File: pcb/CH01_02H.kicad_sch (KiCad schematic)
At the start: 10 parts

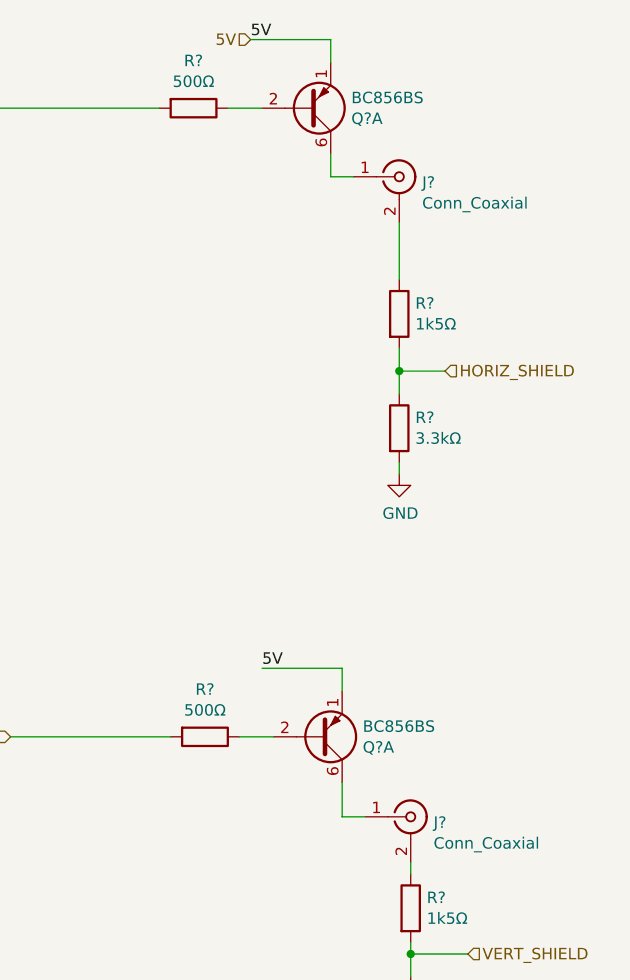
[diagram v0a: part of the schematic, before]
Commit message: Corrections to the coax driver
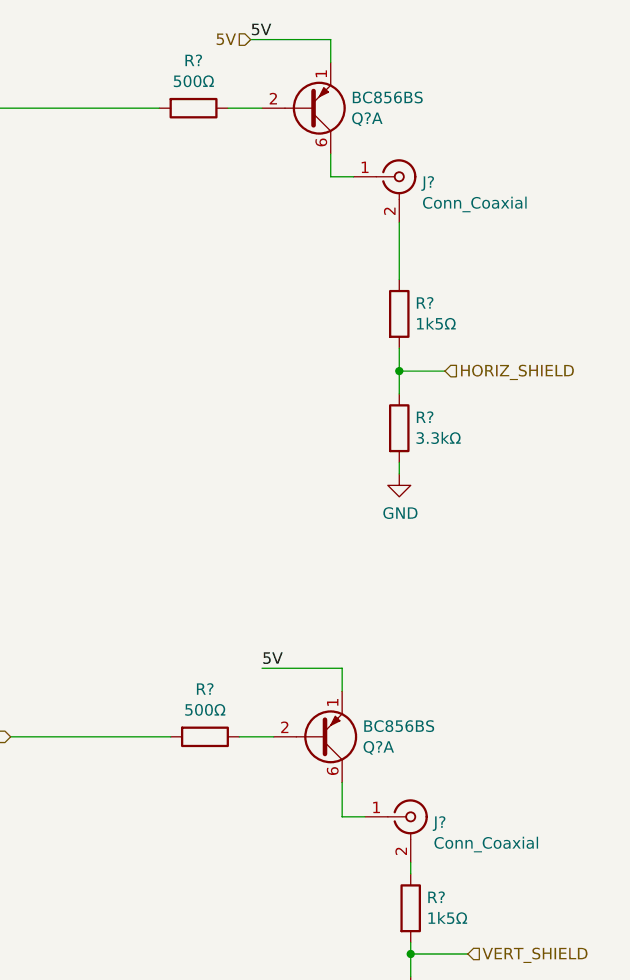
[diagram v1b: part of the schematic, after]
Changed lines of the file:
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@@
     (effects (font (size 1.27 1.27)) (justify right))
   )
-  (symbol (lib_id "Device:R") (at 116.84 87.63 0)
+  (symbol (lib_id "Device:R") (at 116.84 87.63 0) (unit 1)
     (in_bom yes) (on_board yes)
     (property "Reference" "R?" (id 0) (at 118.618 86.4616 0)
@@
     (pin "2")
   )
-  (symbol (lib_id "Device:R") (at 118.11 140.97 0)
+  (symbol (lib_id "Device:R") (at 118.11 140.97 0) (unit 1)
     (in_bom yes) (on_board yes)
     (property "Reference" "R?" (id 0) (at 119.888 139.8016 0)
@@
     (pin "2")
   )
-  (symbol (lib_id "power:GND") (at 118.11 157.48 0)
+  (symbol (lib_id "power:GND") (at 118.11 157.48 0) (unit 1)
     (in_bom yes) (on_board yes)
     (property "Reference" "#PWR?" (id 0) (at 118.11 163.83 0)
@@
     (pin "1")
   )
-  (symbol (lib_id "Device:R") (at 118.11 152.4 0)
+  (symbol (lib_id "Device:R") (at 118.11 152.4 0) (unit 1)
     (in_bom yes) (on_board yes)
     (property "Reference" "R?" (id 0) (at 119.888 151.2316 0)
@@
     (pin "2")
   )
-  (symbol (lib_id "Connector:Conn_Coaxial") (at 116.84 59.69 0)
+  (symbol (lib_id "Connector:Conn_Coaxial") (at 116.84 59.69 0) (unit 1)
     (in_bom yes) (on_board yes)
     (property "Reference" "J?" (id 0) (at 119.38 60.325 0)
@@
     (pin "2")
   )
-  (symbol (lib_id "Device:R") (at 93.98 52.07 270)
+  (symbol (lib_id "Device:R") (at 93.98 52.07 270) (unit 1)
     (in_bom yes) (on_board yes)
     (property "Reference" "R?" (id 0) (at 93.98 46.8122 90))
@@
     (pin "2")
   )
-  (symbol (lib_id "Device:R") (at 116.84 74.93 0)
+  (symbol (lib_id "Device:R") (at 116.84 74.93 0) (unit 1)
     (in_bom yes) (on_board yes)
     (property "Reference" "R?" (id 0) (at 118.618 73.7616 0)
@@
     (pin "2")
   )
-  (symbol (lib_id "Transistor_BJT:BC856BS") (at 106.68 52.07 0) (mirror x)
+  (symbol (lib_id "Transistor_BJT:BC856BS") (at 106.68 52.07 0) (mirror x) (unit 1)
     (in_bom yes) (on_board yes)
     (property "Reference" "Q?" (id 0) (at 111.506 53.2384 0)
@@
     (pin "6")
   )
-  (symbol (lib_id "power:GND") (at 116.84 92.71 0)
+  (symbol (lib_id "power:GND") (at 116.84 92.71 0) (unit 1)
     (in_bom yes) (on_board yes)
     (property "Reference" "#PWR?" (id 0) (at 116.84 99.06 0)
@@
     (pin "1")
   )
-  (symbol (lib_id "Connector:Conn_Coaxial") (at 118.11 130.81 0)
+  (symbol (lib_id "Connector:Conn_Coaxial") (at 118.11 130.81 0) (unit 1)
     (in_bom yes) (on_board yes)
     (property "Reference" "J?" (id 0) (at 120.65 131.445 0)
@@
     (pin "2")
   )
-  (symbol (lib_id "Device:R") (at 95.25 121.92 270)
+  (symbol (lib_id "Device:R") (at 95.25 121.92 270) (unit 1)
     (in_bom yes) (on_board yes)
     (property "Reference" "R?" (id 0) (at 95.25 116.6622 90))
@@
     (pin "2")
   )
-  (symbol (lib_id "Transistor_BJT:BC856BS") (at 107.95 121.92 0) (mirror x)
+  (symbol (lib_id "Transistor_BJT:BC856BS") (at 107.95 121.92 0) (mirror x) (unit 1)
     (in_bom yes) (on_board yes)
     (property "Reference" "Q?" (id 0) (at 112.776 123.0884 0)
@@
       (effects (font (size 1.27 1.27)) hide)
     )
-    (pin "3")
-    (pin "4")
-    (pin "5")
+    (pin "1")
+    (pin "2")
+    (pin "6")
   )
 )

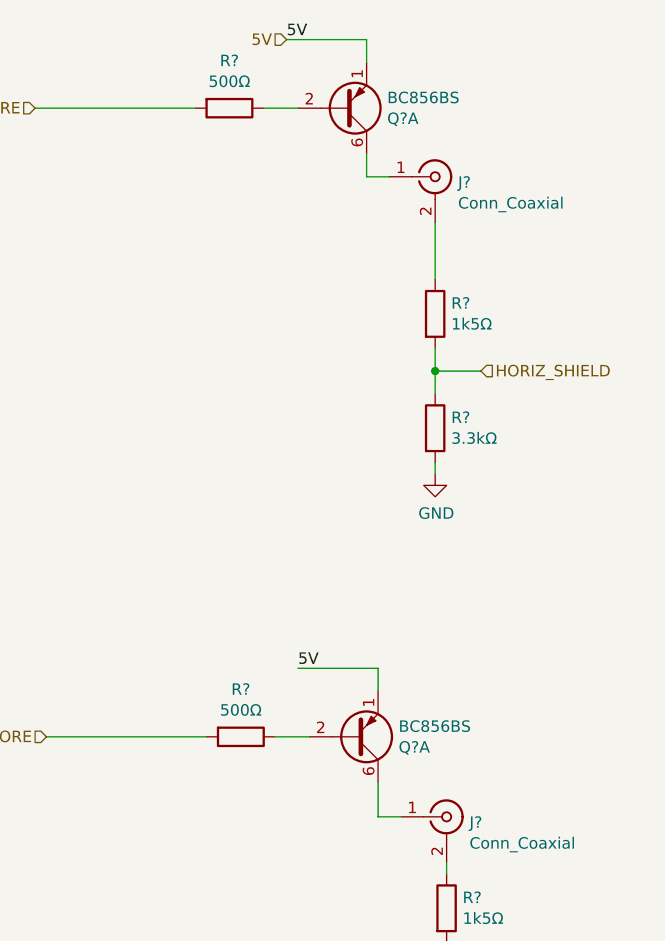
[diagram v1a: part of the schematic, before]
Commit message: Shift register updates - changes the driver from pnp to npn
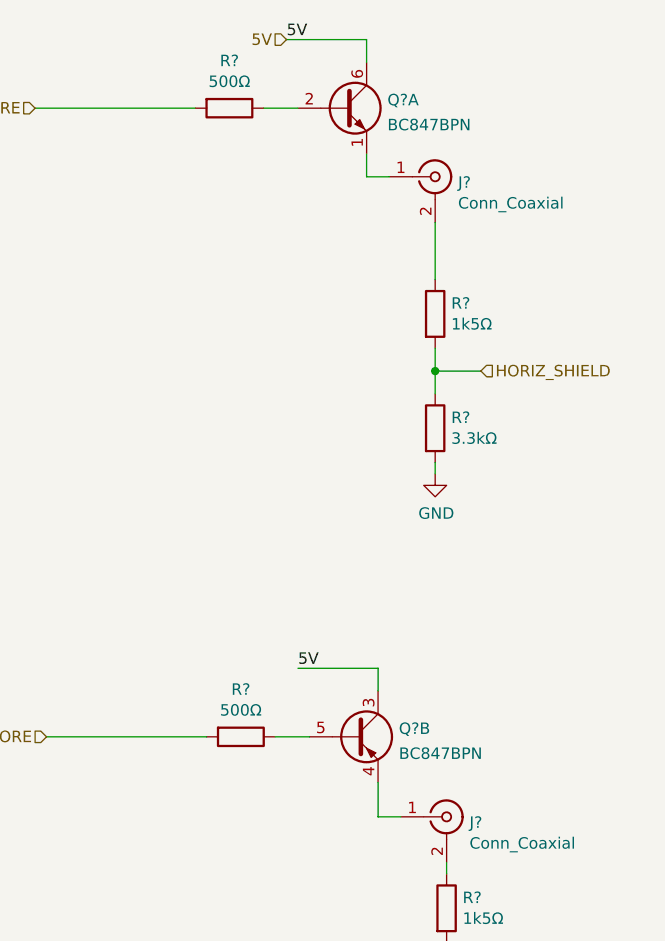
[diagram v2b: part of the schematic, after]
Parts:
- removed Q? (x2): BC856BS, Package_TO_SOT_SMD:SOT-363_SC-70-6, symbol Transistor_BJT:BC856BS
- added Q? (x2): BC847BPN, Package_TO_SOT_SMD:SOT-363_SC-70-6, symbol Transistor_BJT:BC847BPN
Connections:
- net 5V: now also Q?.3 (C2), Q?.6 (C1)
- net at J?.1 (In): now also Q?.1 (E1)
- net at R?.1: now also Q?.2 (B1)
- net at J?.1 (In): now also Q?.4 (E2)
- net at R?.1: now also Q?.5 (B2)
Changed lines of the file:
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@@
     (pin "2")
-  )
-  (symbol (lib_id "Transistor_BJT:BC856BS") (at 106.68 52.07 0) (mirror x) (unit 1)
-    (in_bom yes) (on_board yes)
-    (property "Reference" "Q?" (id 0) (at 111.506 53.2384 0)
-      (effects (font (size 1.27 1.27)) (justify left))
-    )
-    (property "Value" "BC856BS" (id 1) (at 111.506 50.927 0)
-      (effects (font (size 1.27 1.27)) (justify left))
-    )
-    (property "Footprint" "Package_TO_SOT_SMD:SOT-363_SC-70-6" (id 2) (at 111.76 54.61 0)
-      (effects (font (size 1.27 1.27)) hide)
-    )
-    (property "Datasheet" "https://assets.nexperia.com/documents/data-sheet/BC856BS.pdf" (id 3) (at 106.68 52.07 0)
-      (effects (font (size 1.27 1.27)) hide)
-    )
-    (pin "1")
-    (pin "2")
-    (pin "6")
   )
   (symbol (lib_id "power:GND") (at 116.84 92.71 0) (unit 1)
@@
     (pin "2")
   )
-  (symbol (lib_id "Transistor_BJT:BC856BS") (at 107.95 121.92 0) (mirror x) (unit 1)
-    (in_bom yes) (on_board yes)
-    (property "Reference" "Q?" (id 0) (at 112.776 123.0884 0)
+  (symbol (lib_id "Transistor_BJT:BC847BPN") (at 106.68 52.07 0) (unit 1)
+    (in_bom yes) (on_board yes) (fields_autoplaced)
+    (property "Reference" "Q?" (id 0) (at 111.5314 51.1615 0)
       (effects (font (size 1.27 1.27)) (justify left))
     )
-    (property "Value" "BC856BS" (id 1) (at 112.776 120.777 0)
+    (property "Value" "BC847BPN" (id 1) (at 111.5314 53.9366 0)
       (effects (font (size 1.27 1.27)) (justify left))
     )
-    (property "Footprint" "Package_TO_SOT_SMD:SOT-363_SC-70-6" (id 2) (at 113.03 124.46 0)
+    (property "Footprint" "Package_TO_SOT_SMD:SOT-363_SC-70-6" (id 2) (at 111.76 49.53 0)
       (effects (font (size 1.27 1.27)) hide)
     )
-    (property "Datasheet" "https://assets.nexperia.com/documents/data-sheet/BC856BS.pdf" (id 3) (at 107.95 121.92 0)
+    (property "Datasheet" "https://assets.nexperia.com/documents/data-sheet/BC847BPN.pdf" (id 3) (at 106.68 52.07 0)
       (effects (font (size 1.27 1.27)) hide)
     )
@@
     (pin "6")
   )
+  (symbol (lib_id "Transistor_BJT:BC847BPN") (at 107.95 121.92 0) (unit 2)
+    (in_bom yes) (on_board yes) (fields_autoplaced)
+    (property "Reference" "Q?" (id 0) (at 112.8014 121.0115 0)
+      (effects (font (size 1.27 1.27)) (justify left))
+    )
+    (property "Value" "BC847BPN" (id 1) (at 112.8014 123.7866 0)
+      (effects (font (size 1.27 1.27)) (justify left))
+    )
+    (property "Footprint" "Package_TO_SOT_SMD:SOT-363_SC-70-6" (id 2) (at 113.03 119.38 0)
+      (effects (font (size 1.27 1.27)) hide)
+    )
+    (property "Datasheet" "https://assets.nexperia.com/documents/data-sheet/BC847BPN.pdf" (id 3) (at 107.95 121.92 0)
+      (effects (font (size 1.27 1.27)) hide)
+    )
+    (pin "3")
+    (pin "4")
+    (pin "5")
+  )
 )

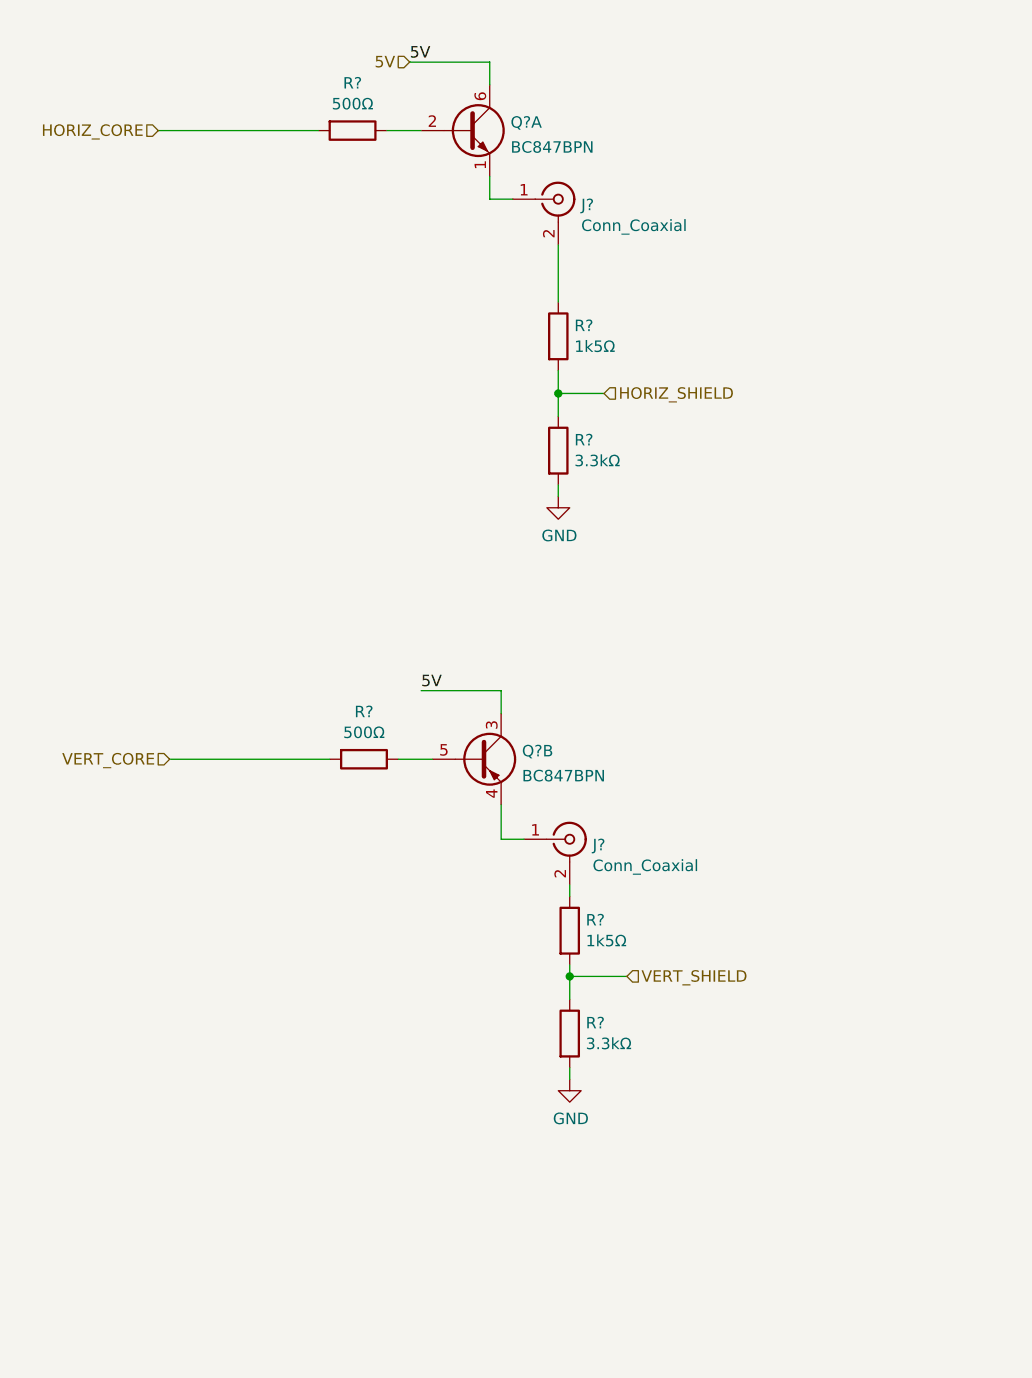
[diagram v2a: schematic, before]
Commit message: Adds line protection
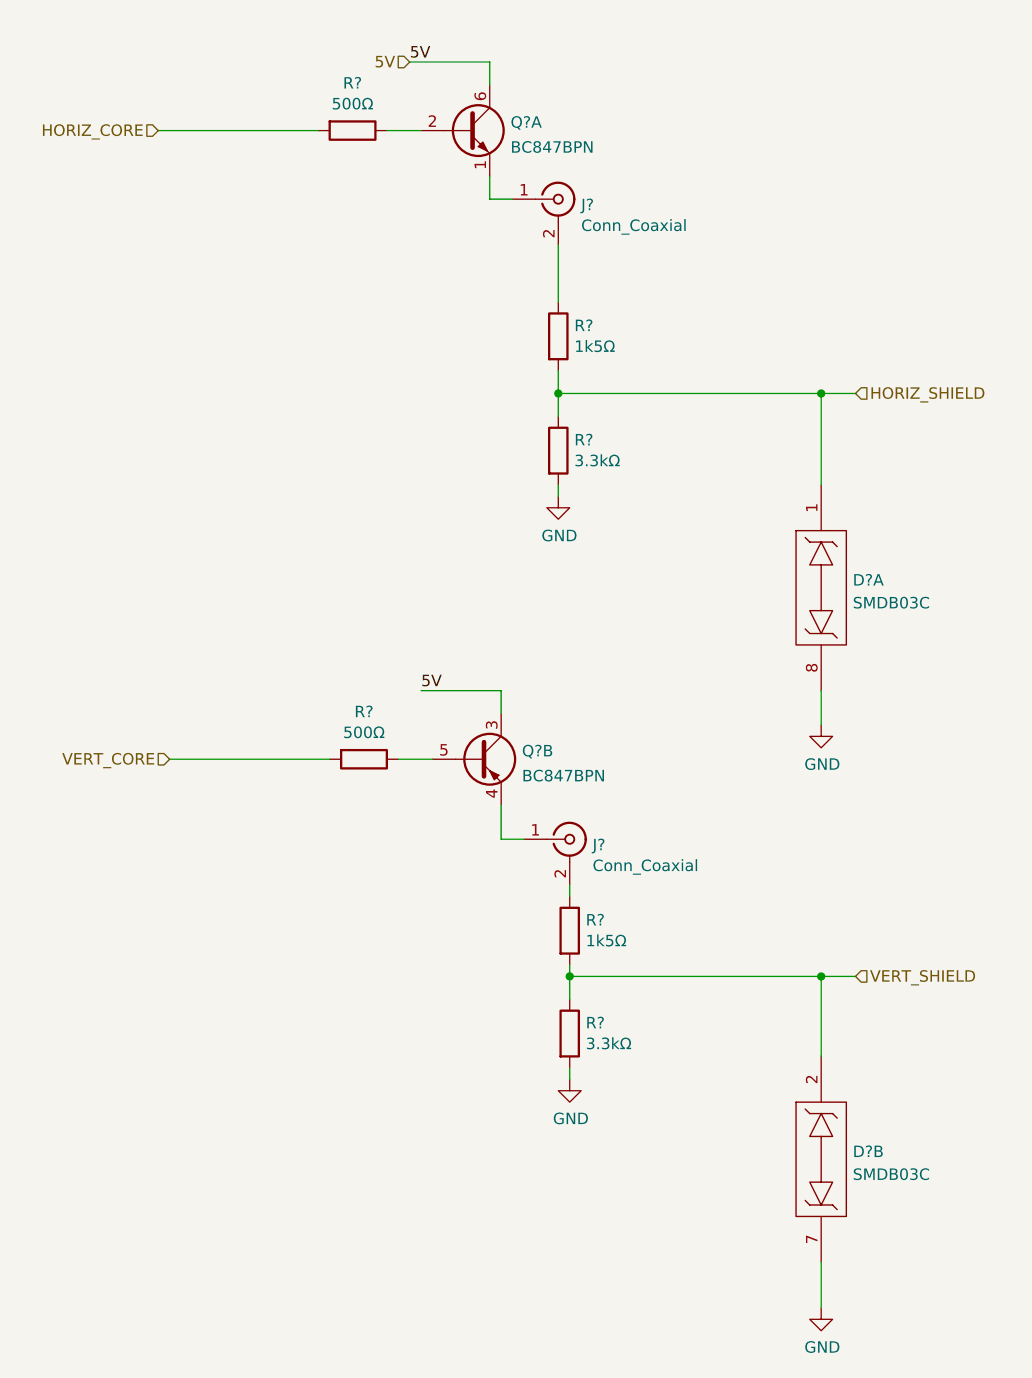
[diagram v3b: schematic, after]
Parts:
- added D? (x2): SMDB03C, Package_SO:SO-8_3.9x4.9mm_P1.27mm, symbol CoaxTester:SMDB03C
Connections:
- net GND: now also D?.7, D?.8
- net HORIZ_SHIELD: now also D?.1
- net VERT_SHIELD: now also D?.2
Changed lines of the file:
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@@
 (kicad_sch (version 20211123) (generator eeschema)
   (paper "A4")
+  (junction (at 146.05 81.28) (diameter 0) (color 0 0 0 0)
+  )
   (junction (at 116.84 81.28) (diameter 0) (color 0 0 0 0)
   )
+  (junction (at 146.05 146.05) (diameter 0) (color 0 0 0 0)
+  )
   (junction (at 118.11 146.05) (diameter 0) (color 0 0 0 0)
   )
+  (wire (pts (xy 146.05 182.88) (xy 146.05 177.8))
+    (stroke (width 0) (type default) (color 0 0 0 0))
+  )
+  (wire (pts (xy 116.84 81.28) (xy 146.05 81.28))
+    (stroke (width 0) (type default) (color 0 0 0 0))
+  )
   (wire (pts (xy 109.22 59.69) (xy 111.76 59.69))
     (stroke (width 0) (type default) (color 0 0 0 0))
@@
     (stroke (width 0) (type default) (color 0 0 0 0))
   )
+  (wire (pts (xy 146.05 81.28) (xy 149.86 81.28))
+    (stroke (width 0) (type default) (color 0 0 0 0))
+  )
+  (wire (pts (xy 146.05 114.3) (xy 146.05 118.11))
+    (stroke (width 0) (type default) (color 0 0 0 0))
+  )
+  (wire (pts (xy 146.05 81.28) (xy 146.05 91.44))
+    (stroke (width 0) (type default) (color 0 0 0 0))
+  )
+  (wire (pts (xy 146.05 154.94) (xy 146.05 146.05))
+    (stroke (width 0) (type default) (color 0 0 0 0))
+  )
   (wire (pts (xy 118.11 144.78) (xy 118.11 146.05))
     (stroke (width 0) (type default) (color 0 0 0 0))
@@
     (stroke (width 0) (type default) (color 0 0 0 0))
   )
-  (wire (pts (xy 116.84 81.28) (xy 121.92 81.28))
+  (wire (pts (xy 146.05 146.05) (xy 149.86 146.05))
     (stroke (width 0) (type default) (color 0 0 0 0))
   )
@@
     (stroke (width 0) (type default) (color 0 0 0 0))
   )
-  (wire (pts (xy 118.11 146.05) (xy 124.46 146.05))
-    (stroke (width 0) (type default) (color 0 0 0 0))
-  )
   (wire (pts (xy 116.84 64.77) (xy 116.84 71.12))
     (stroke (width 0) (type default) (color 0 0 0 0))
@@
   )
   (wire (pts (xy 73.66 121.92) (xy 91.44 121.92))
+    (stroke (width 0) (type default) (color 0 0 0 0))
+  )
+  (wire (pts (xy 118.11 146.05) (xy 146.05 146.05))
     (stroke (width 0) (type default) (color 0 0 0 0))
   )
@@
     (effects (font (size 1.27 1.27)) (justify left bottom))
   )
-  (hierarchical_label "HORIZ_SHIELD" (shape input) (at 121.92 81.28 0)
+  (hierarchical_label "HORIZ_SHIELD" (shape input) (at 149.86 81.28 0)
     (effects (font (size 1.27 1.27)) (justify left))
   )
-  (hierarchical_label "VERT_SHIELD" (shape input) (at 124.46 146.05 0)
+  (hierarchical_label "VERT_SHIELD" (shape input) (at 149.86 146.05 0)
     (effects (font (size 1.27 1.27)) (justify left))
   )
@@
     (pin "2")
   )
+  (symbol (lib_id "power:GND") (at 146.05 182.88 0) (unit 1)
+    (in_bom yes) (on_board yes)
+    (property "Reference" "#PWR?" (id 0) (at 146.05 189.23 0)
+      (effects (font (size 1.27 1.27)) hide)
+    )
+    (property "Value" "GND" (id 1) (at 146.177 187.2742 0))
+    (property "Footprint" "" (id 2) (at 146.05 182.88 0)
+      (effects (font (size 1.27 1.27)) hide)
+    )
+    (property "Datasheet" "" (id 3) (at 146.05 182.88 0)
+      (effects (font (size 1.27 1.27)) hide)
+    )
+    (pin "1")
+  )
   (symbol (lib_id "Transistor_BJT:BC847BPN") (at 106.68 52.07 0) (unit 1)
     (in_bom yes) (on_board yes) (fields_autoplaced)
@@
     (pin "5")
   )
+  (symbol (lib_id "CoaxTester:SMDB03C") (at 146.05 102.87 0) (unit 1)
+    (in_bom yes) (on_board yes) (fields_autoplaced)
+    (property "Reference" "D?" (id 0) (at 149.5552 102.0353 0)
+      (effects (font (size 1.27 1.27)) (justify left))
+    )
+    (property "Value" "SMDB03C" (id 1) (at 149.5552 104.5722 0)
+      (effects (font (size 1.27 1.27)) (justify left))
+    )
+    (property "Footprint" "Package_SO:SO-8_3.9x4.9mm_P1.27mm" (id 2) (at 146.05 101.6 0)
+      (effects (font (size 1.27 1.27)) hide)
+    )
+    (property "Datasheet" "https://www.smc-diodes.com/propdf/SMDB03C%20THRU%20SMDB24C%20N0426%20REV.A.pdf" (id 3) (at 146.05 101.6 0)
+      (effects (font (size 1.27 1.27)) hide)
+    )
+    (pin "1")
+    (pin "8")
+  )
+  (symbol (lib_id "power:GND") (at 146.05 118.11 0) (unit 1)
+    (in_bom yes) (on_board yes)
+    (property "Reference" "#PWR?" (id 0) (at 146.05 124.46 0)
+      (effects (font (size 1.27 1.27)) hide)
+    )
+    (property "Value" "GND" (id 1) (at 146.177 122.5042 0))
+    (property "Footprint" "" (id 2) (at 146.05 118.11 0)
+      (effects (font (size 1.27 1.27)) hide)
+    )
+    (property "Datasheet" "" (id 3) (at 146.05 118.11 0)
+      (effects (font (size 1.27 1.27)) hide)
+    )
+    (pin "1")
+  )
+  (symbol (lib_id "CoaxTester:SMDB03C") (at 146.05 166.37 0) (unit 2)
+    (in_bom yes) (on_board yes) (fields_autoplaced)
+    (property "Reference" "D?" (id 0) (at 149.5552 165.5353 0)
+      (effects (font (size 1.27 1.27)) (justify left))
+    )
+    (property "Value" "SMDB03C" (id 1) (at 149.5552 168.0722 0)
+      (effects (font (size 1.27 1.27)) (justify left))
+    )
+    (property "Footprint" "Package_SO:SO-8_3.9x4.9mm_P1.27mm" (id 2) (at 146.05 165.1 0)
+      (effects (font (size 1.27 1.27)) hide)
+    )
+    (property "Datasheet" "https://www.smc-diodes.com/propdf/SMDB03C%20THRU%20SMDB24C%20N0426%20REV.A.pdf" (id 3) (at 146.05 165.1 0)
+      (effects (font (size 1.27 1.27)) hide)
+    )
+    (pin "2")
+    (pin "7")
+  )
 )
